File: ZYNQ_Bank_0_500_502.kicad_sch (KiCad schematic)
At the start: 49 parts, among them J10 Conn_01x06_Socket, SW1 DSIC02LSGET, SW2 SW-1825027-5, U21 CH340N, U22 MAX809TTRG, U23 W25Q256FVEIG, U8 XC7Z020-CLG484

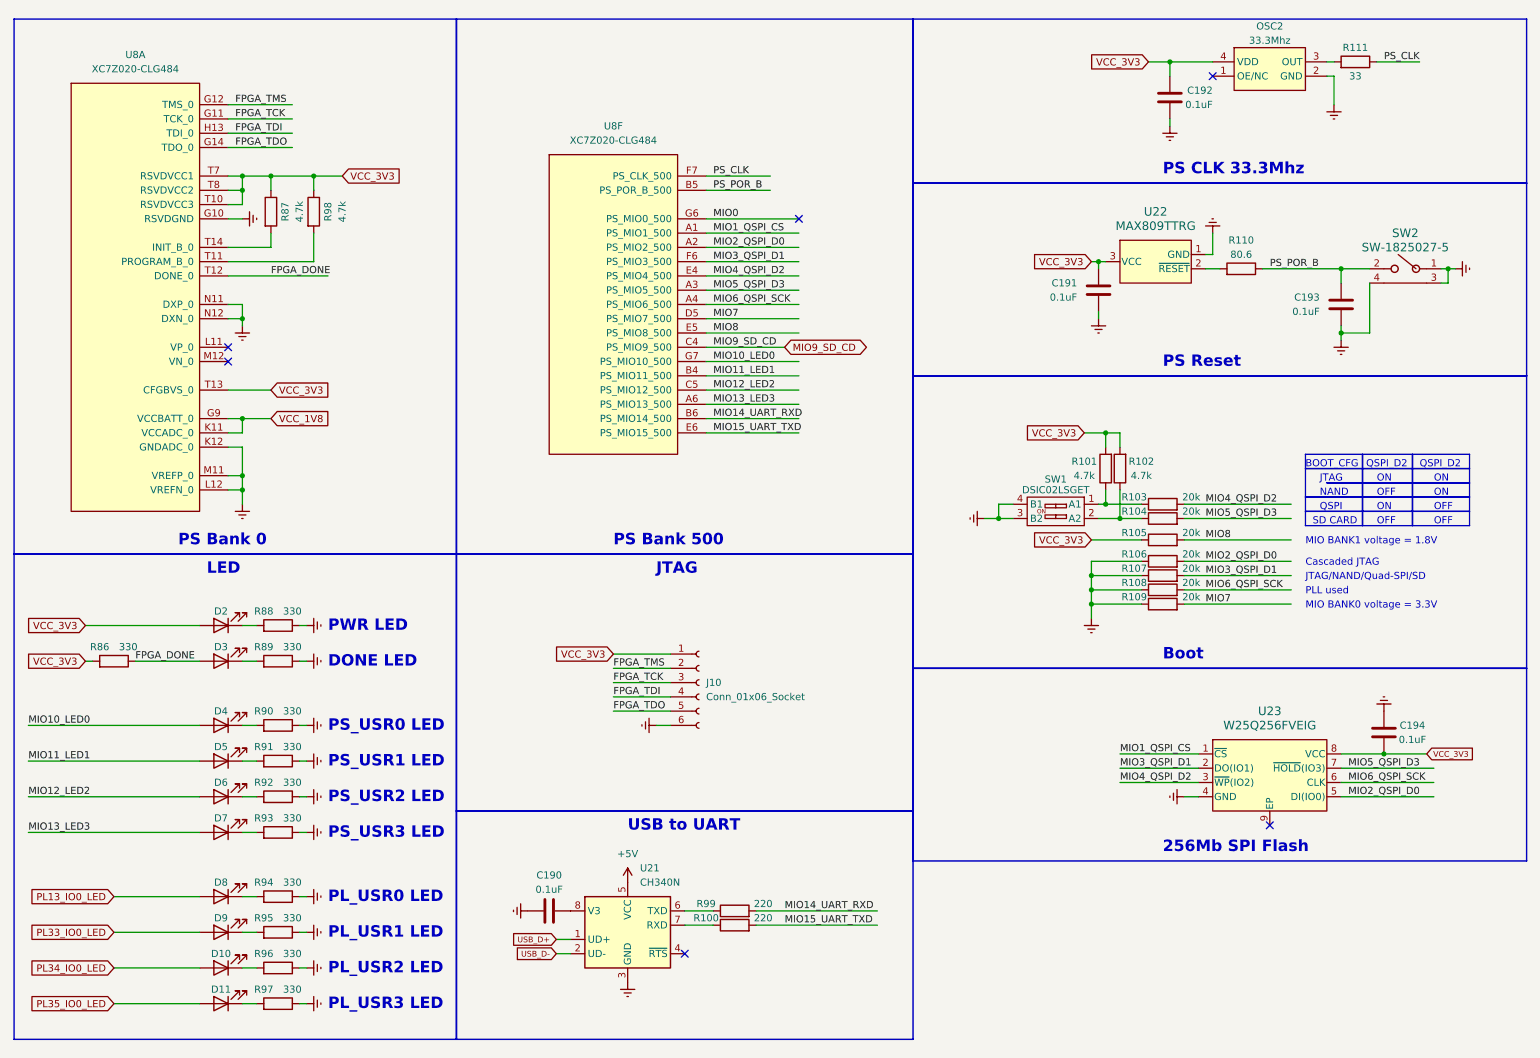
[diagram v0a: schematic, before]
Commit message: 变压器输入+两块DDR3
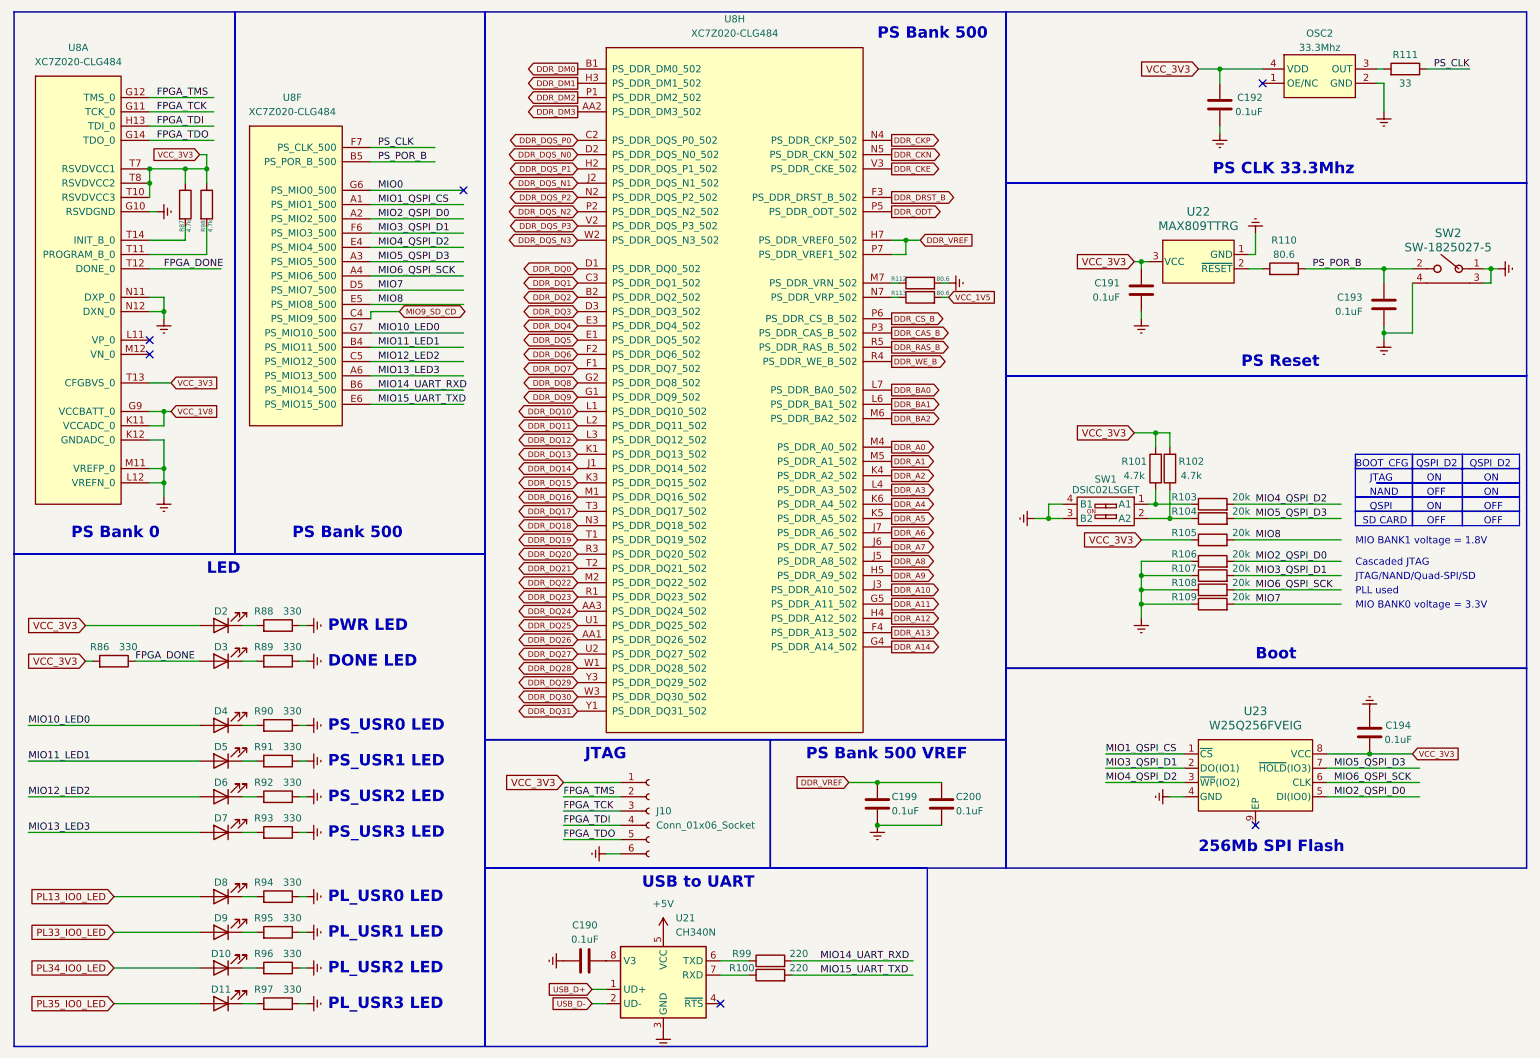
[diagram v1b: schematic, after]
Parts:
- added C199, C200: 0.1uF, Capacitor_SMD:C_0402_1005Metric, symbol Device:C
- added R112, R113: 80.6, Resistor_SMD:R_0402_1005Metric, symbol Device:R
- added unit 8 of U8
- SW2: footprint footprints:SW_1825027-5 -> SW2_1825027-A_TEC
- U22: footprint Package_TO_SOT_SMD:SOT-23 -> SOT-23_ONS
- U23: footprint Package_SON:WSON-8-1EP_8x6mm_P1.27mm_EP3.4x4.3mm -> WIN_E-8_WIN
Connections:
- net Earth: now also C199.1, C200.1, R112.2
- new net: R112.1, U8.M7 (PS_DDR_VRN_502)
- new net: R113.1, U8.N7 (PS_DDR_VRP_502)
- new net DDR_A0: U8.M4 (PS_DDR_A0_502)
- new net DDR_A1: U8.M5 (PS_DDR_A1_502)
- new net DDR_A10: U8.J3 (PS_DDR_A10_502)
- new net DDR_A11: U8.G5 (PS_DDR_A11_502)
- new net DDR_A12: U8.H4 (PS_DDR_A12_502)
- new net DDR_A13: U8.F4 (PS_DDR_A13_502)
- new net DDR_A14: U8.G4 (PS_DDR_A14_502)
- new net DDR_A2: U8.K4 (PS_DDR_A2_502)
- new net DDR_A3: U8.L4 (PS_DDR_A3_502)
- new net DDR_A4: U8.K6 (PS_DDR_A4_502)
- new net DDR_A5: U8.K5 (PS_DDR_A5_502)
- new net DDR_A6: U8.J7 (PS_DDR_A6_502)
- new net DDR_A7: U8.J6 (PS_DDR_A7_502)
- new net DDR_A8: U8.J5 (PS_DDR_A8_502)
- new net DDR_A9: U8.H5 (PS_DDR_A9_502)
- new net DDR_BA0: U8.L7 (PS_DDR_BA0_502)
- new net DDR_BA1: U8.L6 (PS_DDR_BA1_502)
- new net DDR_BA2: U8.M6 (PS_DDR_BA2_502)
- new net DDR_CAS_B: U8.P3 (PS_DDR_CAS_B_502)
- new net DDR_CKE: U8.V3 (PS_DDR_CKE_502)
- new net DDR_CKN: U8.N5 (PS_DDR_CKN_502)
- new net DDR_CKP: U8.N4 (PS_DDR_CKP_502)
- new net DDR_CS_B: U8.P6 (PS_DDR_CS_B_502)
- new net DDR_DM0: U8.B1 (PS_DDR_DM0_502)
- new net DDR_DM1: U8.H3 (PS_DDR_DM1_502)
- new net DDR_DM2: U8.P1 (PS_DDR_DM2_502)
- new net DDR_DM3: U8.AA2 (PS_DDR_DM3_502)
- new net DDR_DQ0: U8.D1 (PS_DDR_DQ0_502)
- new net DDR_DQ1: U8.C3 (PS_DDR_DQ1_502)
- new net DDR_DQ10: U8.L1 (PS_DDR_DQ10_502)
- new net DDR_DQ11: U8.L2 (PS_DDR_DQ11_502)
- new net DDR_DQ12: U8.L3 (PS_DDR_DQ12_502)
- new net DDR_DQ13: U8.K1 (PS_DDR_DQ13_502)
- new net DDR_DQ14: U8.J1 (PS_DDR_DQ14_502)
- new net DDR_DQ15: U8.K3 (PS_DDR_DQ15_502)
- new net DDR_DQ16: U8.M1 (PS_DDR_DQ16_502)
- new net DDR_DQ17: U8.T3 (PS_DDR_DQ17_502)
- new net DDR_DQ18: U8.N3 (PS_DDR_DQ18_502)
- new net DDR_DQ19: U8.T1 (PS_DDR_DQ19_502)
- new net DDR_DQ2: U8.B2 (PS_DDR_DQ2_502)
- new net DDR_DQ20: U8.R3 (PS_DDR_DQ20_502)
- new net DDR_DQ21: U8.T2 (PS_DDR_DQ21_502)
- new net DDR_DQ22: U8.M2 (PS_DDR_DQ22_502)
- new net DDR_DQ23: U8.R1 (PS_DDR_DQ23_502)
- new net DDR_DQ24: U8.AA3 (PS_DDR_DQ24_502)
- new net DDR_DQ25: U8.U1 (PS_DDR_DQ25_502)
- new net DDR_DQ26: U8.AA1 (PS_DDR_DQ26_502)
- new net DDR_DQ27: U8.U2 (PS_DDR_DQ27_502)
- new net DDR_DQ28: U8.W1 (PS_DDR_DQ28_502)
- new net DDR_DQ29: U8.Y3 (PS_DDR_DQ29_502)
- new net DDR_DQ3: U8.D3 (PS_DDR_DQ3_502)
- new net DDR_DQ30: U8.W3 (PS_DDR_DQ30_502)
- new net DDR_DQ31: U8.Y1 (PS_DDR_DQ31_502)
- new net DDR_DQ4: U8.E3 (PS_DDR_DQ4_502)
- new net DDR_DQ5: U8.E1 (PS_DDR_DQ5_502)
- new net DDR_DQ6: U8.F2 (PS_DDR_DQ6_502)
- new net DDR_DQ7: U8.F1 (PS_DDR_DQ7_502)
- new net DDR_DQ8: U8.G2 (PS_DDR_DQ8_502)
- new net DDR_DQ9: U8.G1 (PS_DDR_DQ9_502)
- new net DDR_DQS_N0: U8.D2 (PS_DDR_DQS_N0_502)
- new net DDR_DQS_N1: U8.J2 (PS_DDR_DQS_N1_502)
- new net DDR_DQS_N2: U8.P2 (PS_DDR_DQS_N2_502)
- new net DDR_DQS_N3: U8.W2 (PS_DDR_DQS_N3_502)
- new net DDR_DQS_P0: U8.C2 (PS_DDR_DQS_P0_502)
- new net DDR_DQS_P1: U8.H2 (PS_DDR_DQS_P1_502)
- new net DDR_DQS_P2: U8.N2 (PS_DDR_DQS_P2_502)
- new net DDR_DQS_P3: U8.V2 (PS_DDR_DQS_P3_502)
- new net DDR_DRST_B: U8.F3 (PS_DDR_DRST_B_502)
- new net DDR_ODT: U8.P5 (PS_DDR_ODT_502)
- new net DDR_RAS_B: U8.R5 (PS_DDR_RAS_B_502)
- new net DDR_VREF: C199.2, C200.2, U8.H7 (PS_DDR_VREF0_502), U8.P7 (PS_DDR_VREF1_502)
- new net DDR_WE_B: U8.R4 (PS_DDR_WE_B_502)
- new net VCC_1V5: R113.2
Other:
- note added: "PS Bank 500 VREF"
- moved on the sheet: C190, C191, C192, C193, C194, J10, OSC2, R100, R101, R102, R103, R104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

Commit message: 删除-5V电源，添加eMMC模块接口
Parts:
- SW2: footprint SW2_1825027-A_TEC -> footprints:SW_1825027-5
- U14: renamed from U22; footprint SOT-23_ONS -> Package_TO_SOT_SMD:SOT-23
- U15: renamed from U23; footprint WIN_E-8_WIN -> Package_SON:WSON-8-1EP_8x6mm_P1.27mm_EP3.4x4.3mm
- renumbered C190 to C186, C199 to C187, C200 to C188, C191 to C189, C192 to C190, C194 to C191, C193 to C192, R86 to R66, R87 to R67, R98 to R68, R88 to R69, R89 to R70, R90 to R71, R91 to R72, R92 to R73, R93 to R74, R94 to R75, R95 to R76, R96 to R77, R97 to R78, R99 to R79, R100 to R80, R112 to R81, R113 to R82, R101 to R83, R102 to R84, R103 to R85, R104 to R86, R105 to R87, R106 to R88, R107 to R89, R108 to R90, R109 to R91, R110 to R92, R111 to R93, U21 to U13
